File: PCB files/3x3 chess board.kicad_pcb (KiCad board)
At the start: 2 copper layers, 125.3 x 114.5 mm, 94 parts, among them J1 Conn_01x03, J10 Conn_01x03, J11 Conn_01x03, J12 Conn_01x03, J13 Conn_01x03, J14 Conn_01x03, J15 Conn_01x03, J16 Conn_01x03, J17 Conn_02x03_Odd_Even, J2 Conn_01x03, J3 Conn_01x03, J4 Conn_01x03, J5 Conn_01x03, J6 Conn_01x03, J7 Conn_01x03, J8 Conn_01x03, J9 Conn_01x03, U1 MCP23S17_SO, U2 MCP23S17_SO, U3 ESP32-S3-WROOM-1

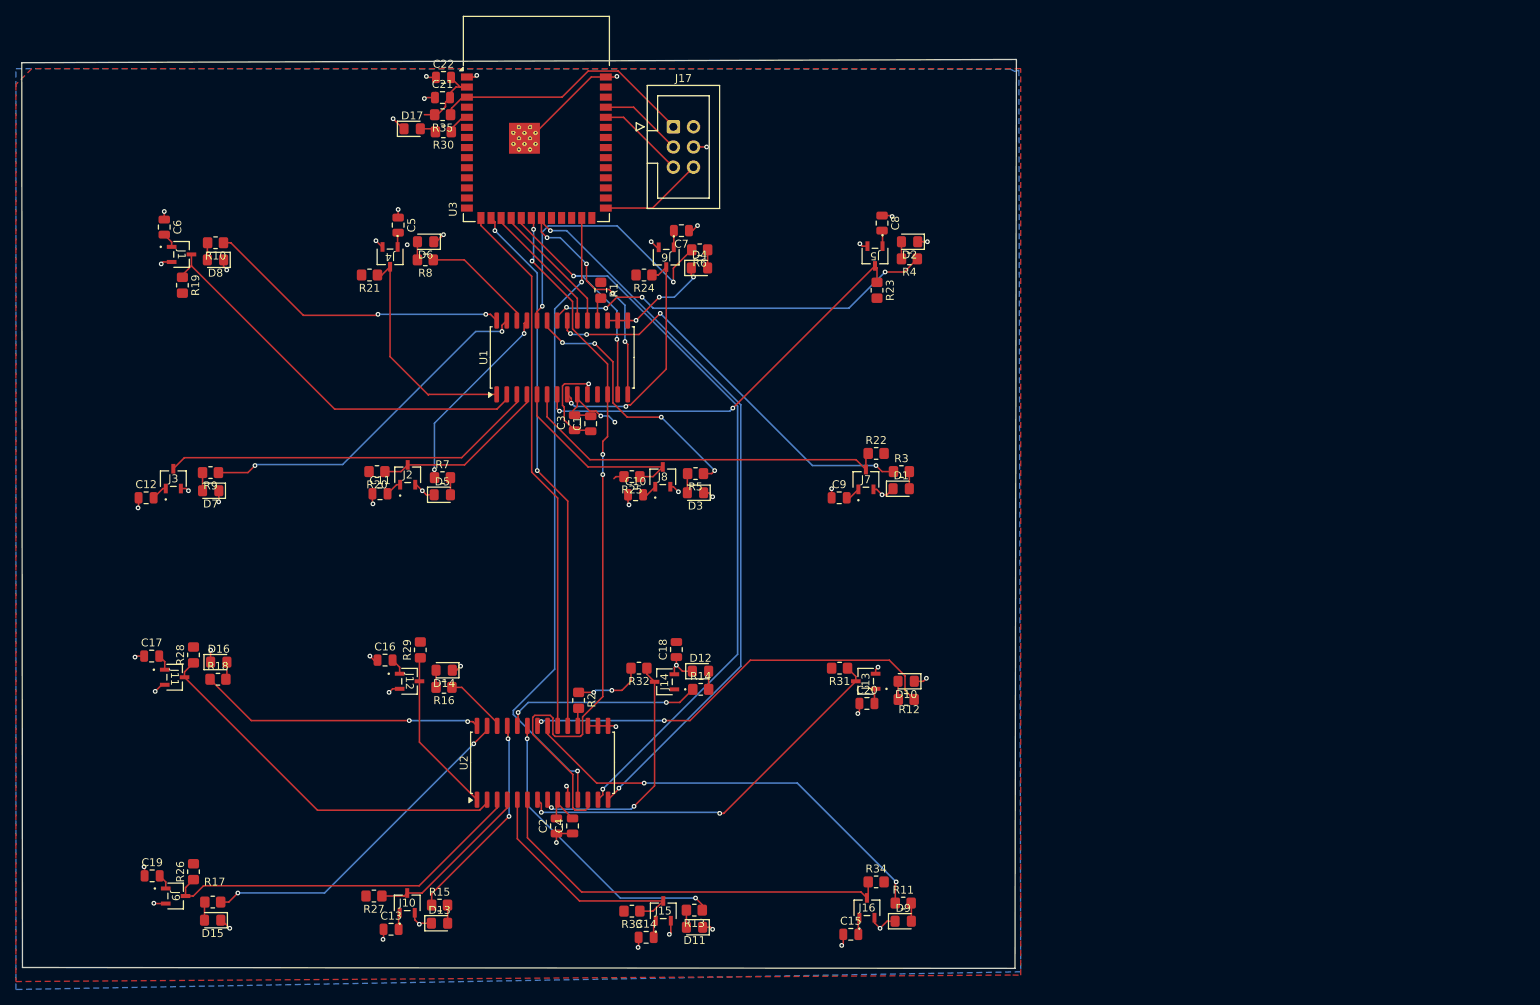
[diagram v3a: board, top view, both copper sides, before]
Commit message: changes
added promotion buttons, removed interrupts, cleaned up silkscreen
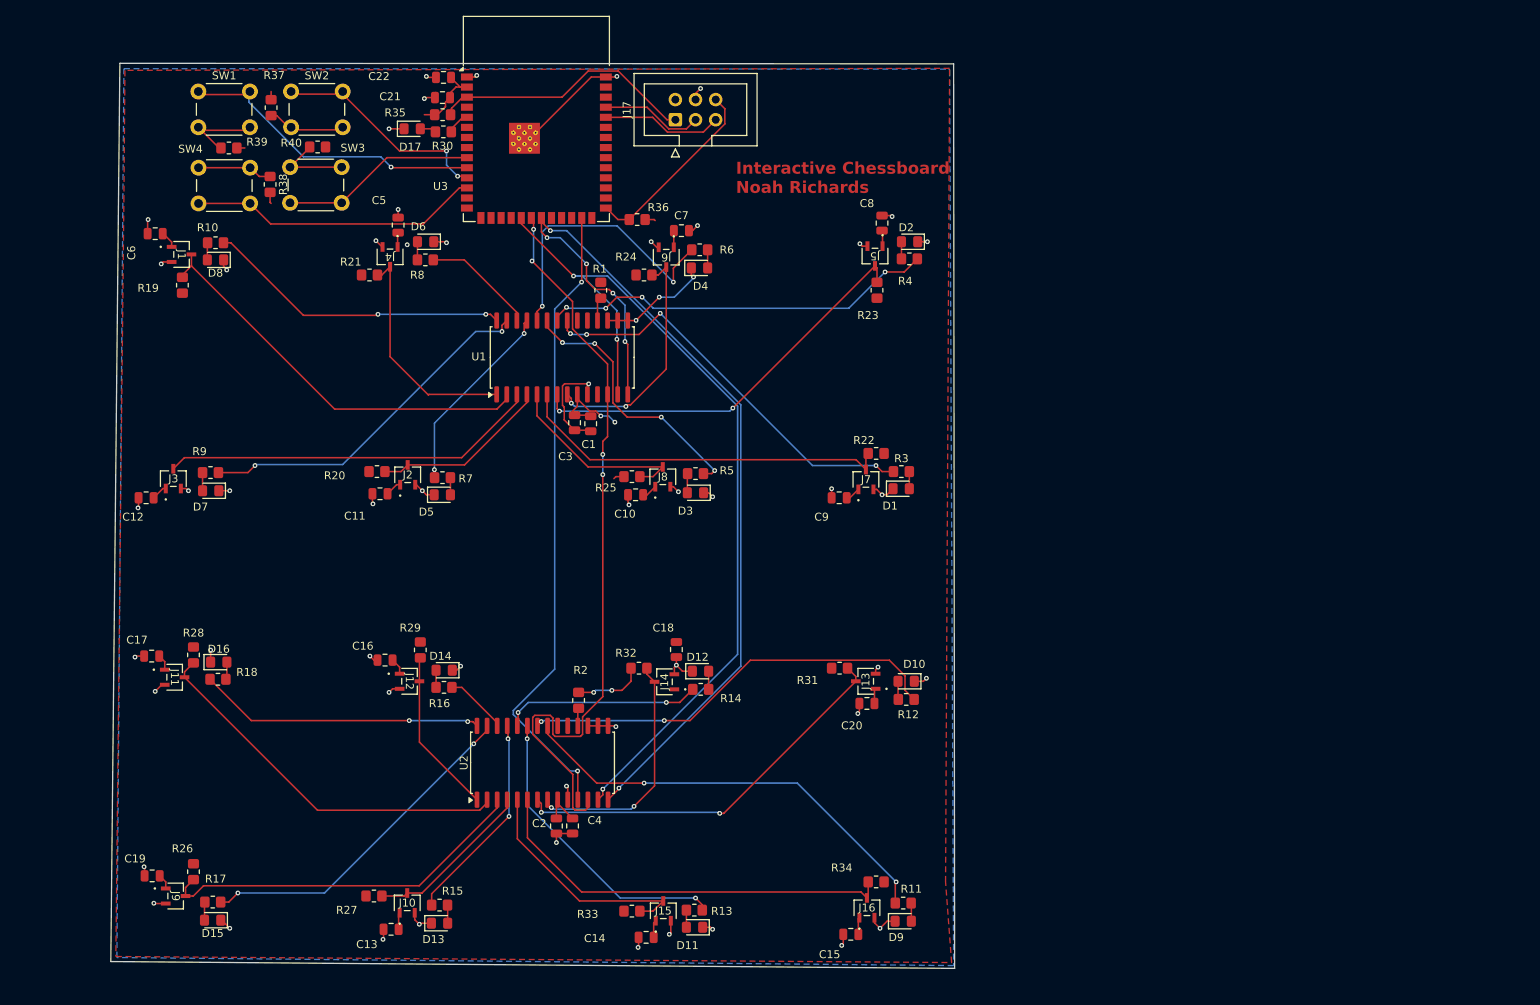
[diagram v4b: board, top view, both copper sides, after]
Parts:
- added R36: 5k, Resistor_SMD:R_0805_2012Metric_Pad1.20x1.40mm_HandSolder, F.Cu at (127.3, 64.0)
- added R37: 10k, Resistor_SMD:R_0805_2012Metric_Pad1.20x1.40mm_HandSolder, F.Cu at (81.2, 49.9)
- added R38: 10k, Resistor_SMD:R_0805_2012Metric_Pad1.20x1.40mm_HandSolder, F.Cu at (81.0, 59.6)
- added R39: 10k, Resistor_SMD:R_0805_2012Metric_Pad1.20x1.40mm_HandSolder, F.Cu at (75.8, 55.0)
- added R40: 10k, Resistor_SMD:R_0805_2012Metric_Pad1.20x1.40mm_HandSolder, F.Cu at (87.0, 54.9)
- added SW1: SW_Push, Button_Switch_THT:SW_PUSH_6mm_H4.3mm, F.Cu at (72.0, 47.9)
- added SW2: SW_Push, Button_Switch_THT:SW_PUSH_6mm_H4.3mm, F.Cu at (83.7, 47.9)
- added SW3: SW_Push, Button_Switch_THT:SW_PUSH_6mm_H4.3mm, F.Cu at (90.0, 61.9)
- added SW4: SW_Push, Button_Switch_THT:SW_PUSH_6mm_H4.3mm, F.Cu at (78.5, 62.0)
- moved C6 1.41 mm to (66.5, 65.8), turned to 0 degrees
- moved J17 0.92 mm to (132.1, 51.4), turned to 90 degrees
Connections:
- U1 pad 19: /INTB_{extender1} -> unconnected-(U1-INTB-Pad19)
- U1 pad 20: /INTA_{extender1} -> unconnected-(U1-INTA-Pad20)
- U2 pad 19: /INTB_{extender2} -> unconnected-(U2-INTB-Pad19)
- U2 pad 20: /INTA_{extender2} -> unconnected-(U2-INTA-Pad20)
- U3 pad 10: unconnected-(U3-IO17-Pad10) -> /Bishop_promote
- U3 pad 11: unconnected-(U3-IO18-Pad11) -> /Rook_promote
- U3 pad 12: unconnected-(U3-IO8-Pad12) -> /Queen_promote
- U3 pad 15: /INTA_{extender2} -> unconnected-(U3-IO3-Pad15)
- U3 pad 16: /INTB_{extender2} -> unconnected-(U3-IO46-Pad16)
- U3 pad 17: /INTA_{extender1} -> unconnected-(U3-IO9-Pad17)
- U3 pad 18: /INTB_{extender1} -> unconnected-(U3-IO10-Pad18)
- U3 pad 9: unconnected-(U3-IO16-Pad9) -> /Knight_promote
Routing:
- net /INTA_{extender2}: track 68.0 -> 0.00 mm
- net /INTB_{extender2}: track 68.0 -> 0.00 mm, vias 2 -> 0
- net /Bishop_promote: track 0.00 -> 38.4 mm, vias 0 -> 1
- net /Queen_promote: track 0.00 -> 36.8 mm
- net /Rook_promote: track 0.00 -> 27.6 mm, vias 0 -> 2
- net /Knight_promote: track 0.00 -> 24.6 mm
- net /INTB_{extender1}: track 16.9 -> 0.00 mm
- net /INTA_{extender1}: track 16.9 -> 0.00 mm
- net /IO0: track 13.2 -> 24.1 mm
- net Net-(R39-Pad1): track 0.00 -> 10.4 mm
- net Net-(R40-Pad1): track 0.00 -> 10.1 mm
- net Net-(R37-Pad1): track 0.00 -> 9.76 mm
- net Net-(R38-Pad1): track 0.00 -> 9.47 mm
- net +3.3V: track 66.9 -> 71.7 mm
- net /RX: track 11.1 -> 15.3 mm
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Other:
- board size 125.3 x 114.5 mm -> 106.3 x 114 mm
- board text added: "Interactive Chessboard Noah Richards"
- board text removed: "MCP23S17_SO"

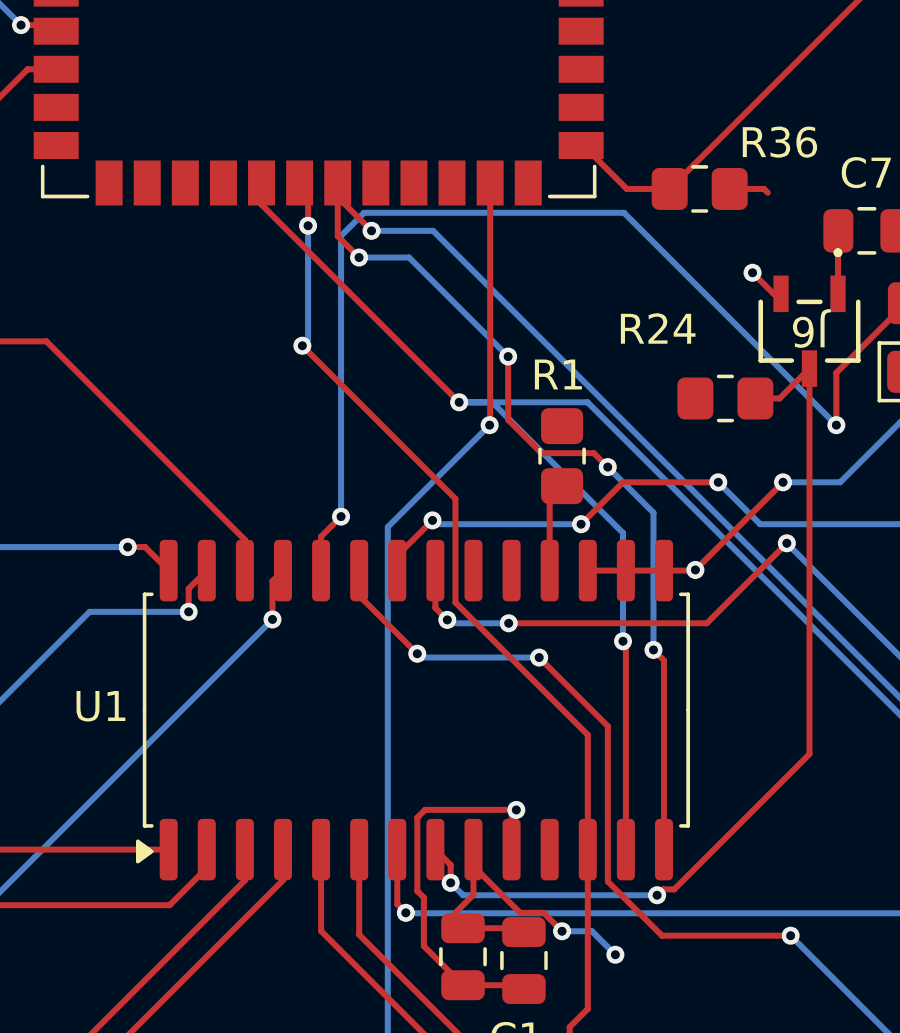
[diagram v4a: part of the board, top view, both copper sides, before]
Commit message: adjustments before ordering
udpated res values, added gerber files and parts list files
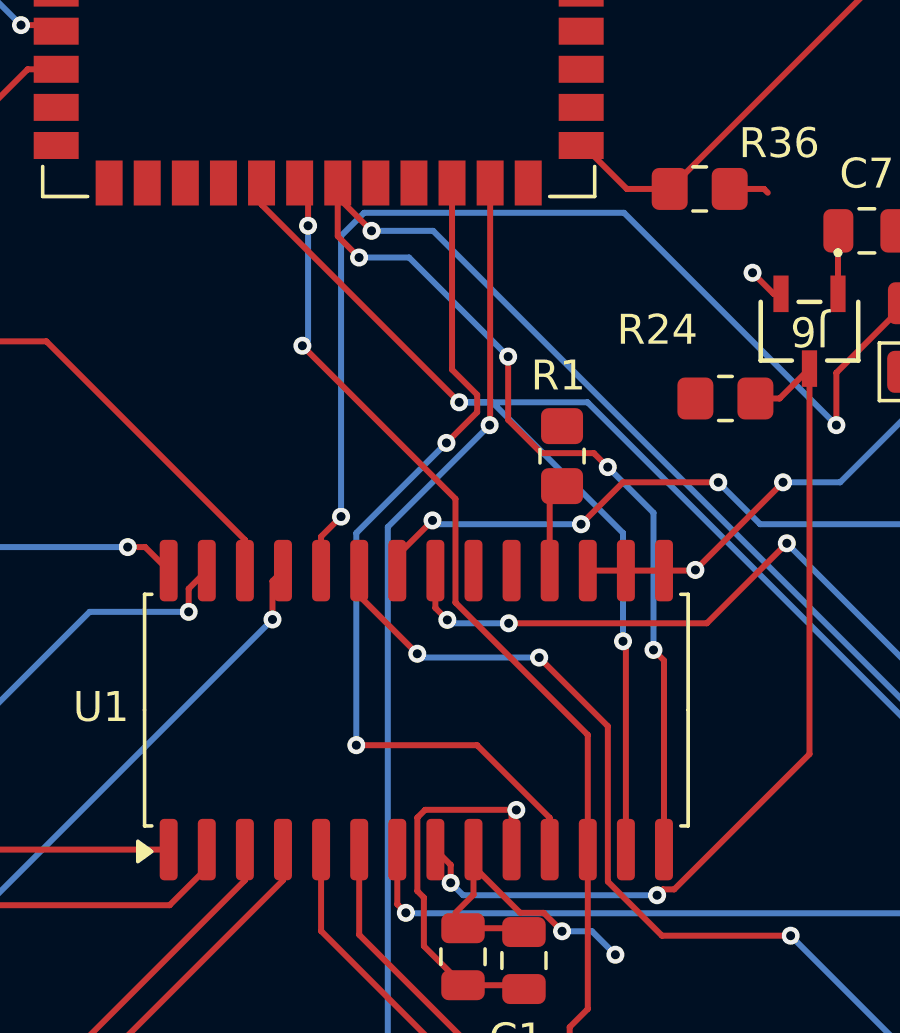
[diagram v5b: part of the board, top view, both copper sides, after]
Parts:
- R10, R11, R12, R13, R14, R15, R16, R17, R18, R3, R4, R5, R6, R7, R8, R9: value 16 -> 150
- R30: value 320 -> 150
- R37, R40: value 10k -> 5k
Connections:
- U1 pad 11: unconnected-(U1-~{CS}-Pad11) -> /CS_{extender1}
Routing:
- net /CS_{extender1}: track 0.00 -> 29.3 mm, vias 0 -> 2
